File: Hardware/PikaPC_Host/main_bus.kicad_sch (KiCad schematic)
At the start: 8 parts, among them J2 DIN41612_03x32_C_Split, J3 Conn_01x03, U2 ATF1508AS, U6 74ALVC164245, Y3 16M

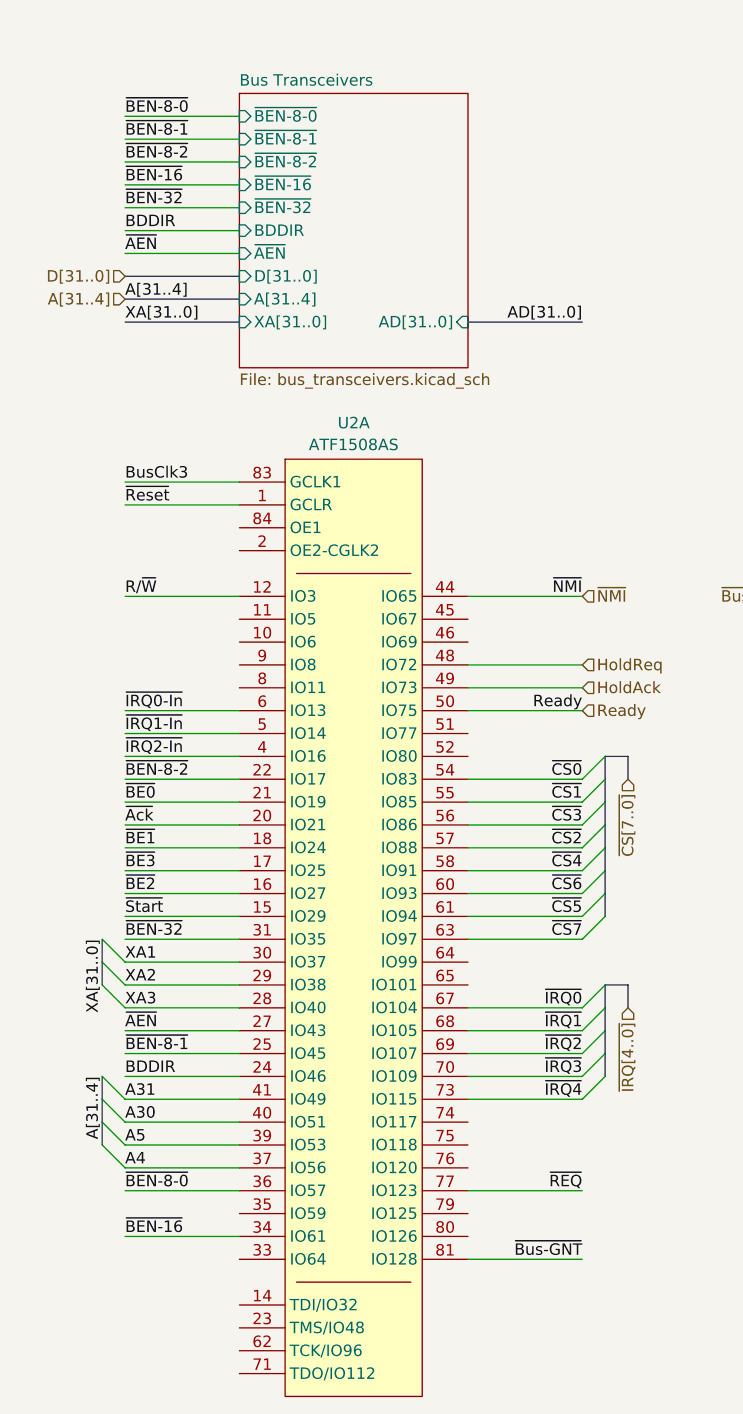
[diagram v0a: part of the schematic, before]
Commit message: fix low two expansion bus address bits
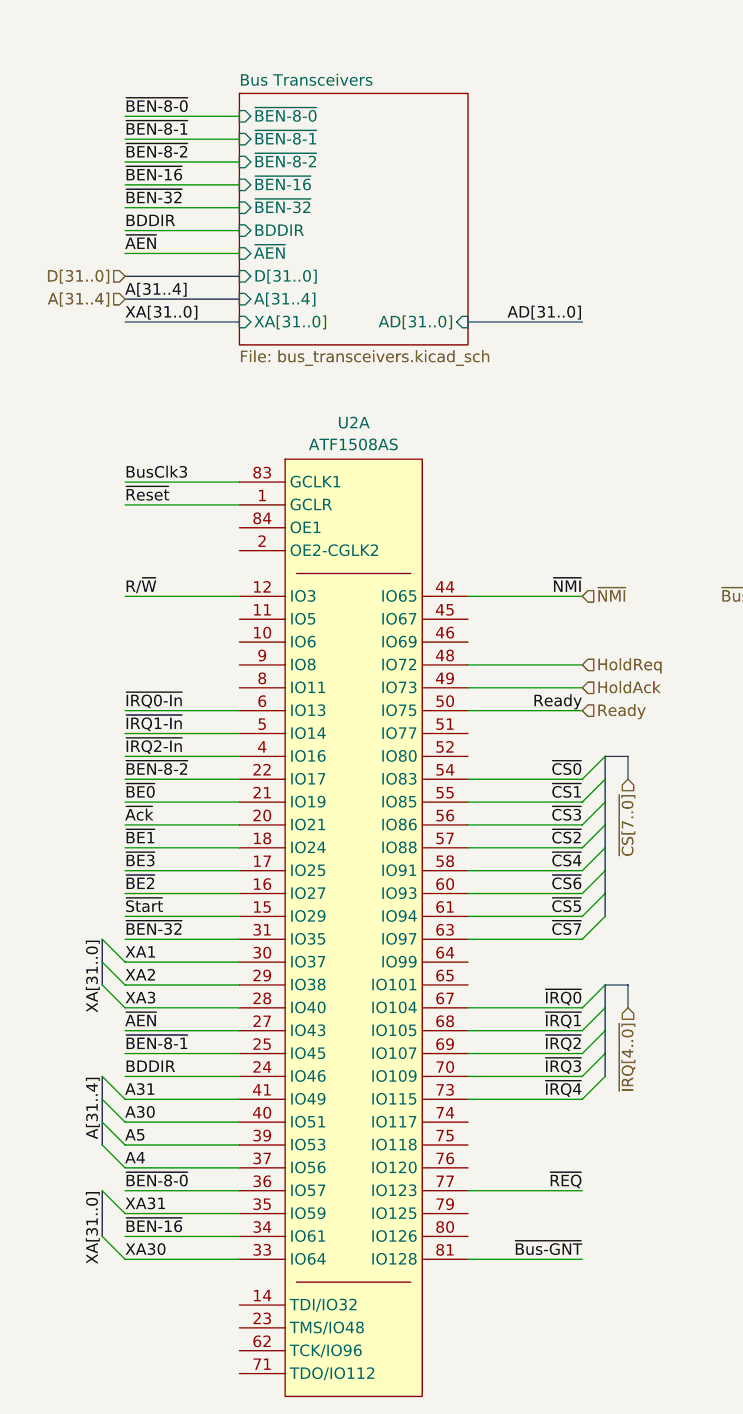
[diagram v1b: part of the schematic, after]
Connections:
- net XA30: now reaches U2.33 (IO64)
- net XA31: now reaches U2.35 (IO59)
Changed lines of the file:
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@@
 	)
 	(bus_entry
+		(at 22.86 147.32)
+		(size 2.54 2.54)
+		(stroke
+			(width 0)
+			(type default)
+		)
+	)
+	(bus_entry
 		(at 78.74 104.14)
 		(size -2.54 2.54)
@@
 	)
 	(bus_entry
+		(at 22.86 142.24)
+		(size 2.54 2.54)
+		(stroke
+			(width 0)
+			(type default)
+		)
+	)
+	(bus_entry
 		(at 78.74 99.06)
 		(size -2.54 2.54)
@@
 	(bus
 		(pts
+			(xy 22.86 142.24) (xy 22.86 147.32)
+		)
+		(stroke
+			(width 0)
+			(type default)
+		)
+	)
+	(bus
+		(pts
 			(xy 25.4 43.18) (xy 38.1 43.18)
 		)
@@
 	(wire
 		(pts
+			(xy 25.4 149.86) (xy 38.1 149.86)
+		)
+		(stroke
+			(width 0)
+			(type default)
+		)
+	)
+	(wire
+		(pts
 			(xy 241.3 53.34) (xy 254 53.34)
 		)
@@
 	(wire
 		(pts
+			(xy 25.4 144.78) (xy 38.1 144.78)
+		)
+		(stroke
+			(width 0)
+			(type default)
+		)
+	)
+	(wire
+		(pts
 			(xy 25.4 139.7) (xy 38.1 139.7)
 		)
@@
 		)
 	)
+	(label "XA31"
+		(at 25.4 144.78 0)
+		(effects
+			(font
+				(size 1.27 1.27)
+			)
+			(justify left bottom)
+		)
+	)
 	(label "~{Bus-BE3}"
 		(at 175.26 78.74 0)
@@
 		)
 	)
+	(label "XA[31..0]"
+		(at 22.86 142.24 270)
+		(effects
+			(font
+				(size 1.27 1.27)
+			)
+			(justify right bottom)
+		)
+	)
 	(label "AD15"
 		(at 175.26 48.26 0)
@@
 		)
 	)
+	(label "XA30"
+		(at 25.4 149.86 0)
+		(effects
+			(font
+				(size 1.27 1.27)
+			)
+			(justify left bottom)
+		)
+	)
 	(label "~{Bus-REQ}"
 		(at 241.3 71.12 0)
@@
 	(sheet
 		(at 38.1 20.32)
-		(size 25.4 30.48)
+		(size 25.4 27.94)
 		(exclude_from_sim no)
 		(in_bom yes)
@@
 		)
 		(property "Sheetfile" "bus_transceivers.kicad_sch"
-			(at 38.1 51.3846 0)
+			(at 38.1 48.8446 0)
 			(effects
 				(font

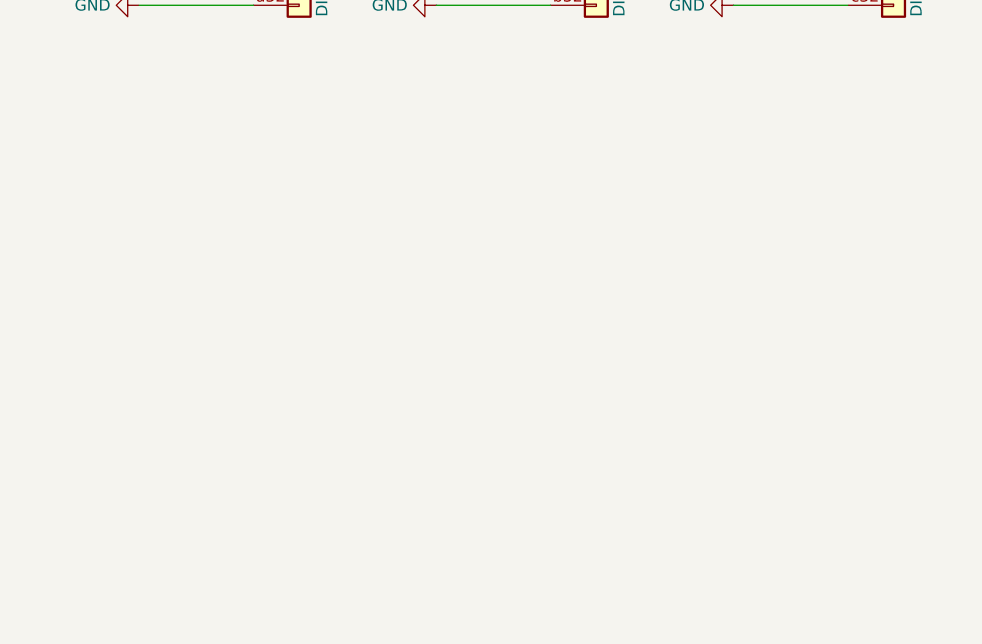
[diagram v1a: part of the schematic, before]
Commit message: don't double-buffer bus clock, add missing bus control signal pull-ups
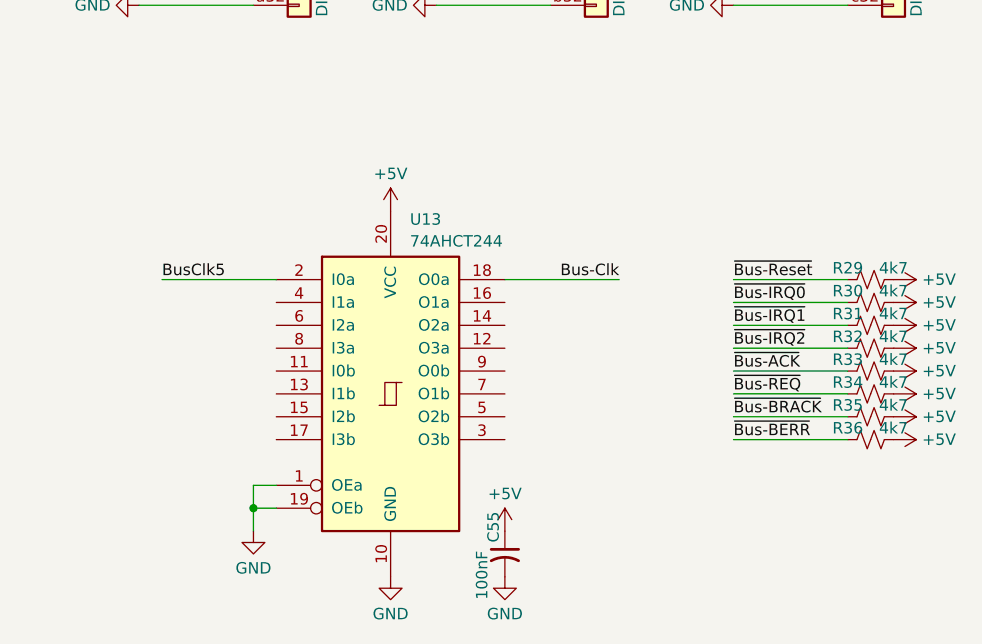
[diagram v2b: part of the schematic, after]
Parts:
- added C55: 100nF, Capacitor_THT:C_Axial_L3.8mm_D2.6mm_P7.50mm_Horizontal, symbol Device:C_Small_US
- added R29, R30, R31, R32, R33, R34, R35, R36: 4k7, Resistor_SMD:R_0805_2012Metric, symbol Device:R_Small_US
- added U13: 74AHCT244, Package_DIP:DIP-20_W7.62mm_Socket, symbol 74xx:74LS244
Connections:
- net +5V: now also C55.1, R29.2, R30.2, R31.2, R32.2, R33.2, R34.2, R35.2, R36.2, U13.20 (VCC)
- net Bus-Clk: now also U13.18 (O0a)
- net BusClk5: now also U13.2 (I0a)
- net GND: now also C55.2, U13.1 (OEa), U13.10 (GND), U13.19 (OEb)
- net ~{Bus-ACK}: now also R33.1
- net ~{Bus-BERR}: now also R36.1
- net ~{Bus-BRACK}: now also R35.1
- net ~{Bus-IRQ0}: now also R30.1
- net ~{Bus-IRQ1}: now also R31.1
- net ~{Bus-IRQ2}: now also R32.1
- net ~{Bus-REQ}: now also R34.1
- net ~{Bus-Reset}: now also R29.1
